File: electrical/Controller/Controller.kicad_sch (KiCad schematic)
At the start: 33 parts, among them J1 USB4145-03-0170-C, J2 TC2030-NL, J3 I2C, Q1 DMP2004K-7, U1 LP5912-3.3DRV, U2 USBLC6-2P6, U3 STM32L072CBTx

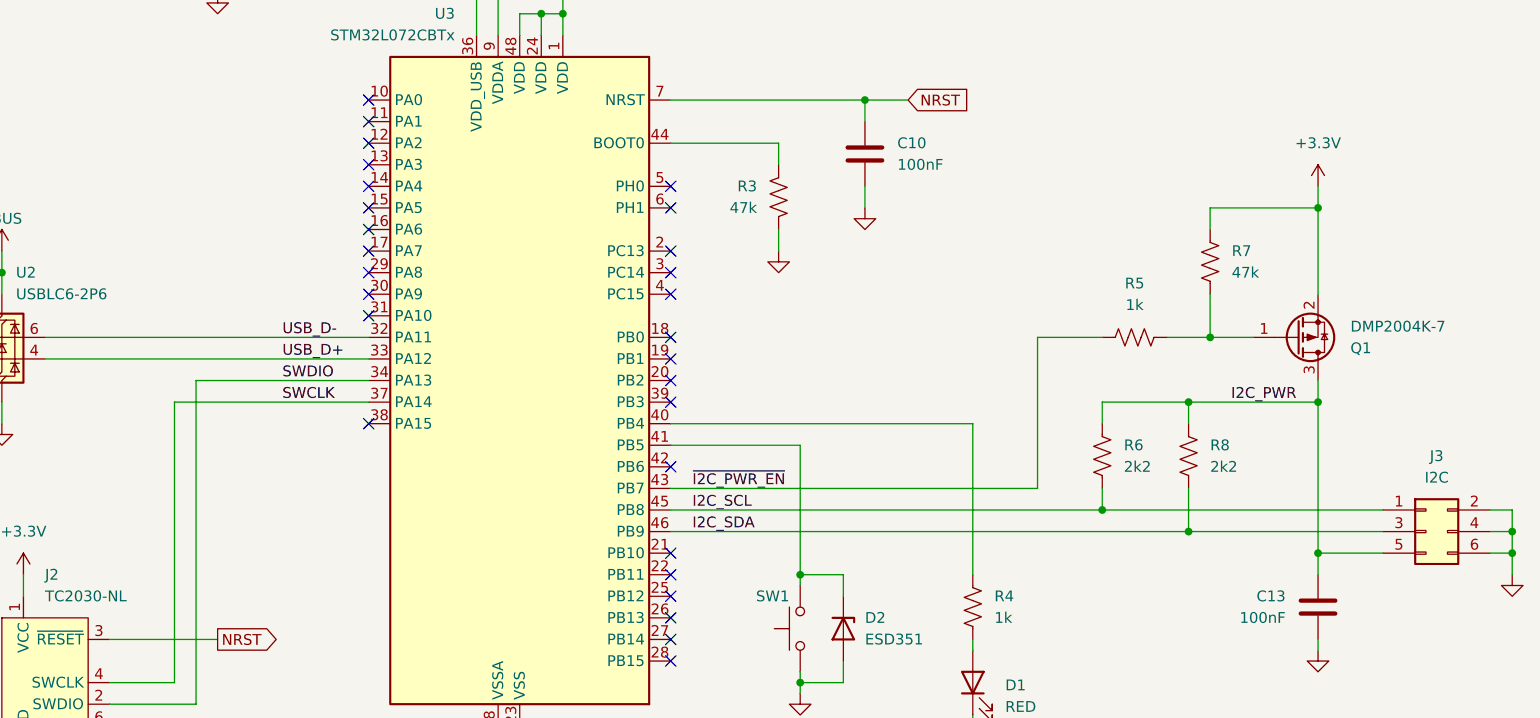
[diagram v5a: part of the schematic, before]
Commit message: Change i2c cable pinout to keep signals between grounds
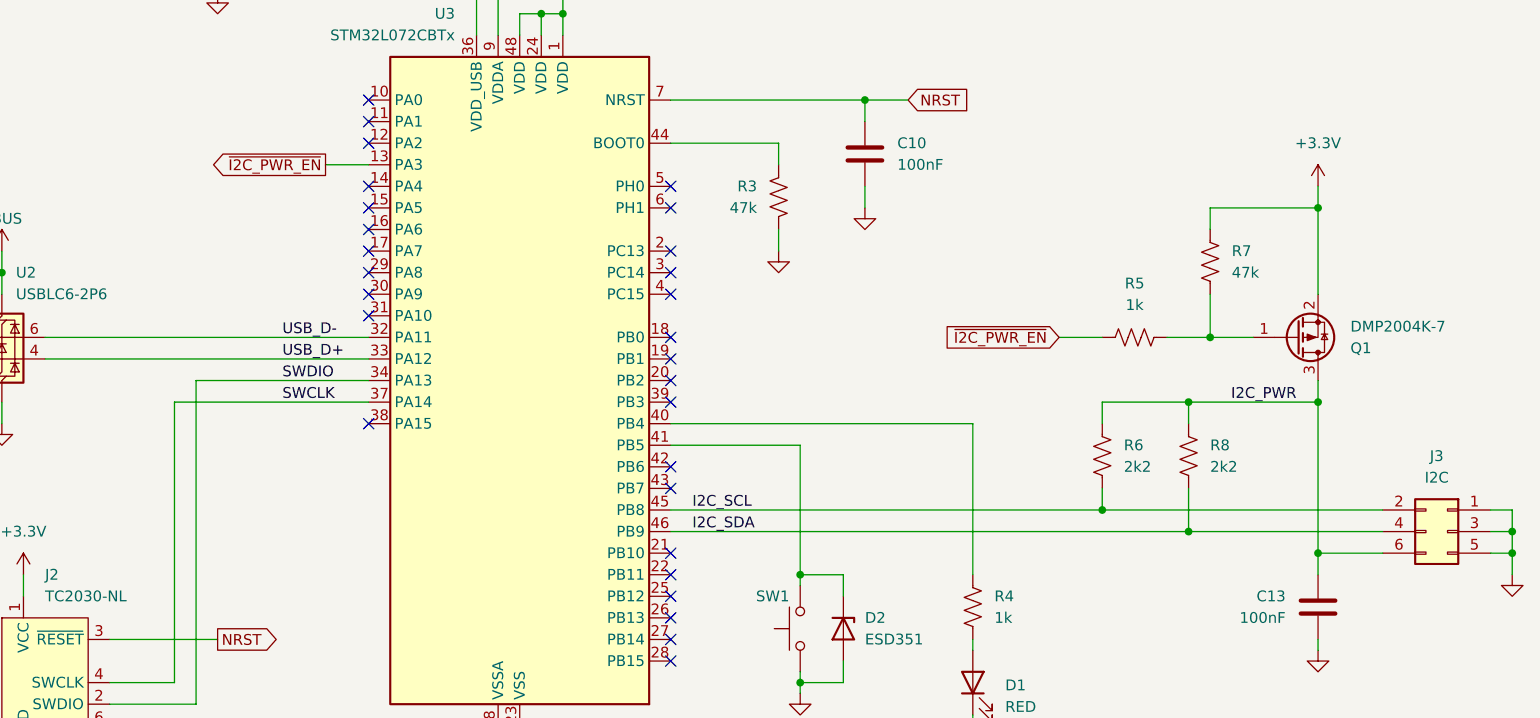
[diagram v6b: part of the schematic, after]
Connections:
- net GND: now also J3.1 (Pin_1), J3.3 (Pin_3), J3.5 (Pin_5); no longer J3.2 (Pin_2), J3.4 (Pin_4), J3.6 (Pin_6)
- net I2C_PWR: now also J3.6 (Pin_6); no longer J3.5 (Pin_5)
- net I2C_SCL: now also J3.2 (Pin_2); no longer J3.1 (Pin_1)
- net I2C_SDA: now also J3.4 (Pin_4); no longer J3.3 (Pin_3)
- net ~{I2C_PWR_EN}: now also U3.13 (PA3); no longer U3.43 (PB7)
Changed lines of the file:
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@@
 	)
 	(no_connect
-		(at 198.12 115.57)
+		(at 233.68 153.67)
 	)
 	(no_connect
@@
 	(wire
 		(pts
-			(xy 276.86 153.67) (xy 276.86 135.89)
-		)
-		(stroke
-			(width 0)
-			(type default)
-		)
-	)
-	(wire
-		(pts
 			(xy 284.48 156.21) (xy 317.5 156.21)
 		)
@@
 	(wire
 		(pts
+			(xy 193.04 115.57) (xy 198.12 115.57)
+		)
+		(stroke
+			(width 0)
+			(type default)
+		)
+	)
+	(wire
+		(pts
 			(xy 220.98 74.93) (xy 236.22 74.93)
 		)
@@
 	(wire
 		(pts
-			(xy 233.68 153.67) (xy 276.86 153.67)
-		)
-		(stroke
-			(width 0)
-			(type default)
-		)
-	)
-	(wire
-		(pts
 			(xy 180.34 57.15) (xy 195.58 57.15)
 		)
@@
 	(wire
 		(pts
-			(xy 276.86 135.89) (xy 284.48 135.89)
+			(xy 279.4 135.89) (xy 284.48 135.89)
 		)
 		(stroke
@@
 		)
 	)
-	(label "~{I2C_PWR_EN}"
-		(at 236.22 153.67 0)
-		(effects
-			(font
-				(size 1.27 1.27)
-			)
-			(justify left bottom)
-		)
-	)
 	(label "I2C_SDA"
 		(at 236.22 158.75 0)
@@
 			)
 			(justify left bottom)
+		)
+	)
+	(global_label "~{I2C_PWR_EN}"
+		(shape input)
+		(at 279.4 135.89 180)
+		(fields_autoplaced yes)
+		(effects
+			(font
+				(size 1.27 1.27)
+			)
+			(justify right)
+		)
+		(property "Intersheetrefs" "${INTERSHEET_REFS}"
+			(at 264.9244 135.89 0)
+			(effects
+				(font
+					(size 1.27 1.27)
+				)
+				(justify right)
+				(hide yes)
+			)
+		)
+	)
+	(global_label "~{I2C_PWR_EN}"
+		(shape output)
+		(at 193.04 115.57 180)
+		(fields_autoplaced yes)
+		(effects
+			(font
+				(size 1.27 1.27)
+			)
+			(justify right)
+		)
+		(property "Intersheetrefs" "${INTERSHEET_REFS}"
+			(at 178.5644 115.57 0)
+			(effects
+				(font
+					(size 1.27 1.27)
+				)
+				(justify right)
+				(hide yes)
+			)
 		)
 	)
@@
 	(symbol
 		(lib_id "Connector_Generic:Conn_02x03_Odd_Even")
-		(at 322.58 158.75 0)
+		(at 325.12 158.75 0)
+		(mirror y)
 		(unit 1)
 		(exclude_from_sim no)
@@
 		(on_board yes)
 		(dnp no)
-		(fields_autoplaced yes)
 		(property "Reference" "J3"
 			(at 323.85 149.86 0)
@@
 		)
 		(property "Footprint" "MidiConcertina:Wuerth_WR-WST_490107670612_2x03_P2.54mm_SKEDD"
-			(at 322.58 158.75 0)
+			(at 325.12 158.75 0)
 			(effects
 				(font
@@
 		)
 		(property "Datasheet" ""
-			(at 322.58 158.75 0)
+			(at 325.12 158.75 0)
 			(effects
 				(font
@@
 		)
 		(property "Description" ""
-			(at 322.58 158.75 0)
-			(effects
-				(font
+			(at 325.12 158.75 0)
+			(effects
+				(font

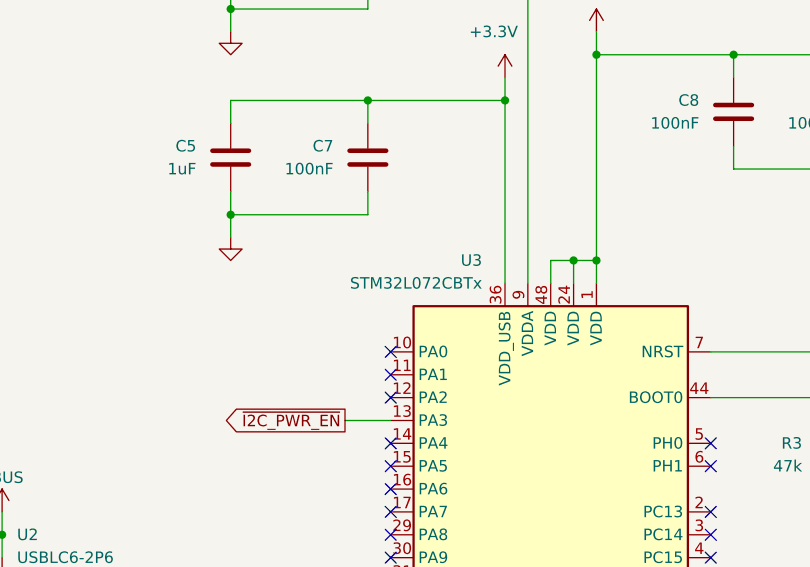
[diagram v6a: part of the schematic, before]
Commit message: Switch to MCU part with more flash for controller board
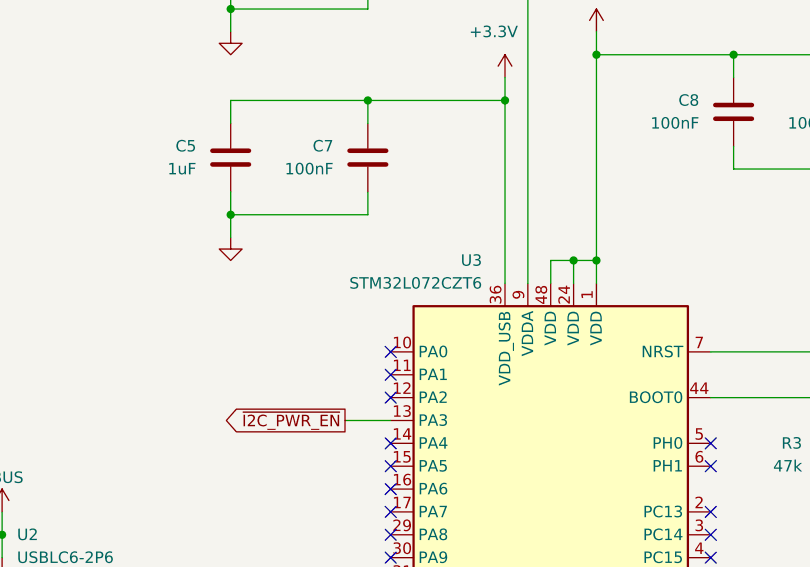
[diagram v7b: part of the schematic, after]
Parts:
- U3: value STM32L072CBTx -> STM32L072CZT6; LCSC C465977 -> C1337587; Part STM32L072CBT6 -> STM32L072CZT6
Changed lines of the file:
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@@
 			)
 		)
-		(property "Value" "STM32L072CBTx"
+		(property "Value" "STM32L072CZT6"
 			(at 208.28 100.33 0)
 			(effects
@@
 			)
 		)
-		(property "Datasheet" "https://www.st.com/resource/en/datasheet/stm32l072cb.pdf"
+		(property "Datasheet" "https://www.st.com/resource/en/datasheet/stm32l072cz.pdf"
 			(at 215.9 140.97 0)
 			(effects
@@
 			)
 		)
-		(property "Description" "STMicroelectronics Arm Cortex-M0+ MCU, 128KB flash, 20KB RAM, 32 MHz, 1.65-3.6V, 37 GPIO, LQFP48"
+		(property "Description" "STMicroelectronics Arm Cortex-M0+ MCU, 192KB flash, 20KB RAM, 32 MHz, 1.65-3.6V, 37 GPIO, LQFP48"
 			(at 215.9 140.97 0)
 			(effects
@@
 			)
 		)
-		(property "LCSC" "C465977"
+		(property "LCSC" "C1337587"
 			(at 215.9 140.97 0)
 			(effects
@@
 			)
 		)
-		(property "Part" "STM32L072CBT6"
+		(property "Part" "STM32L072CZT6"
 			(at 215.9 140.97 0)
 			(effects
